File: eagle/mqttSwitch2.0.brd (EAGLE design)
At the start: 40.3 x 26 mm, 18 parts, among them IC1 AMS117 3.3, K1 G5LE, T1 2N3904

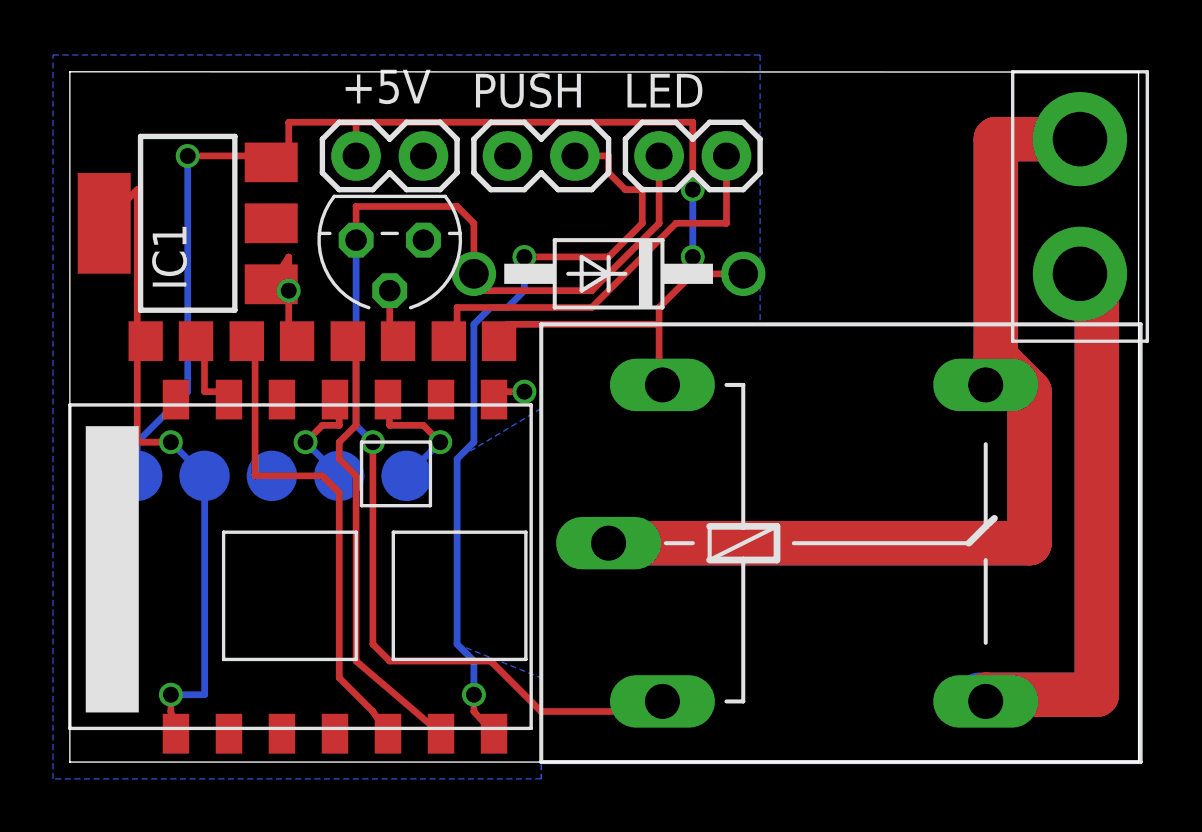
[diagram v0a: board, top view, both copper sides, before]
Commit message: Updated to NPN, Started on KiCad
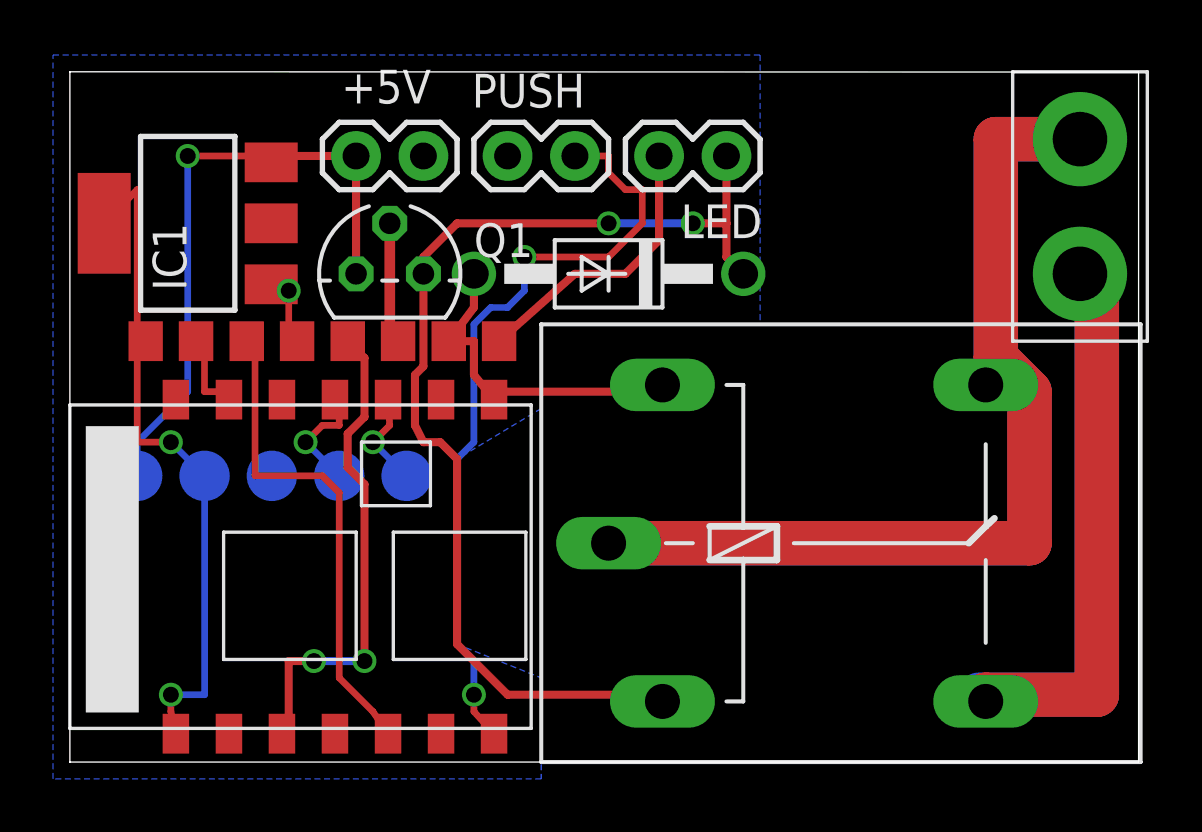
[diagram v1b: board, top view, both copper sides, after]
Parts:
- removed T1: 2N3904, transistor:TO92
- added Q1: 2N3906, transistor-pnp:TO92
- moved LED 2.54 mm to (24.1, 62.2), turned to 180 degrees
- turned R1 to 0 degrees
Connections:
- removed net N$12 (its old number): +5V.2, 5.0V.TP, D1.C, IC1.3, K1.2, R1.1
- removed net N$4: R5.1, U$1.GPIO2
- new net N$13: R5.1, U$1.GPIO12
- new net N$8: D1.C, K1.1, LED.1, Q1.1
- net GND: now also D1.A, K1.2, R1.1; no longer T1.3
- net N$5: now also +5V.2, 5.0V.TP, IC1.3, Q1.3; no longer D1.A, K1.1, LED.1, T1.1
- net N$6: now also Q1.2; no longer T1.2
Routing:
- net N$12 (its old number): track 53.3 -> 0.00 mm, vias 3 -> 0
- net N$8: track 0.00 -> 40.9 mm, vias 0 -> 2
- net N$5: track 46.6 -> 23.7 mm
- net N$13: track 0.00 -> 18.6 mm, vias 0 -> 2
- net N$4: track 16.9 -> 0.00 mm
- net GND: track 6.07 -> 15.8 mm, vias 2 -> 1
- net N$12: track 15.4 -> 10.7 mm
- net N$6: track 1.98 -> 4.52 mm
- net N$9: track 4.94 -> 3.67 mm
